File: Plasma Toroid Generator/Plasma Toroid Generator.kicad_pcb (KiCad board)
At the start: 2 copper layers, 66 x 41 mm, 15 parts, among them J1 Conn_01x02, J2 Conn_01x01, J3 Conn_01x01, J4 Conn_01x01, J5 Conn_01x01, Q1 IRFP260

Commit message: Updated PCB layout to fix errors in cap placement
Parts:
- moved C1 4.19 mm to (170.0, 105.4), turned to 180 degrees
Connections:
- C1 pad 1: Net-(C1-Pad1) -> +15V
- J1 pad 1: Net-(C1-Pad1) -> GND
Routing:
- net +15V: track 31.4 -> 45.8 mm
- net Net-(C1-Pad1): track 11.6 -> 0.00 mm
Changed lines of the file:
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@@
   )
   (net 0 "")
-  (net 1 "Net-(C1-Pad1)")
+  (net 1 "Net-(J3-Pad1)")
   (net 2 "GND")
   (net 3 "Net-(C2-Pad1)")
@@
   (net 5 "Net-(D1-Pad1)")
   (net 6 "+15V")
-  (net 7 "Net-(Q1-Pad2)")
-  (net 8 "Net-(R2-Pad2)")
+  (net 7 "Net-(R2-Pad2)")
   (footprint "Capacitor_THT:C_Rect_L7.2mm_W2.5mm_P5.00mm_FKS2_FKP2_MKS2_MKP2" (layer "F.Cu")
     (at 216 111.5 90)
@@
   )
   (footprint "Capacitor_THT:CP_Radial_D10.0mm_P5.00mm" (layer "F.Cu")
-    (at 166 106.632323 -90)
+    (at 170.007677 105.41 180)
     (descr "CP, Radial series, Radial, pin pitch=5.00mm, , diameter=10mm, Electrolytic Capacitor")
     (tags "CP Radial series Radial pin pitch 5.00mm  diameter 10mm Electrolytic Capacitor")
@@
     (property "Sheetname" "")
     (attr through_hole)
-    (fp_text reference "C1" (at 1 -6.25 180) (layer "F.SilkS")
-      (effects (font (size 1 1) (thickness 0.15)))
-    )
-    (fp_text value "10u" (at 2.5 6.25 90) (layer "F.Fab") hide
-      (effects (font (size 1 1) (thickness 0.15)))
-    )
-    (fp_text user "${REFERENCE}" (at 2.5 0 90) (layer "F.Fab")
+    (fp_text reference "C1" (at 1 -6.25 90) (layer "F.SilkS")
+      (effects (font (size 1 1) (thickness 0.15)))
+    )
+    (fp_text value "10u" (at 2.5 6.25) (layer "F.Fab") hide
+      (effects (font (size 1 1) (thickness 0.15)))
+    )
+    (fp_text user "${REFERENCE}" (at 2.5 0) (layer "F.Fab")
       (effects (font (size 1 1) (thickness 0.15)))
     )
@@
     (fp_line (start -1.788861 -2.1875) (end -0.788861 -2.1875) (layer "F.Fab") (width 0.1))
     (fp_circle (center 2.5 0) (end 7.5 0) (layer "F.Fab") (width 0.1) (fill none))
-    (pad "1" thru_hole rect (at 0 0 270) (size 2 2) (drill 1) (layers *.Cu *.Mask)
-      (net 1 "Net-(C1-Pad1)") (pintype "passive"))
-    (pad "2" thru_hole circle (at 5 0 270) (size 2 2) (drill 1) (layers *.Cu *.Mask)
+    (pad "1" thru_hole rect (at 0 0 180) (size 2 2) (drill 1) (layers *.Cu *.Mask)
+      (net 6 "+15V") (pintype "passive"))
+    (pad "2" thru_hole circle (at 5 0 180) (size 2 2) (drill 1) (layers *.Cu *.Mask)
       (net 2 "GND") (pintype "passive"))
     (model "${KICAD6_3DMODEL_DIR}/Capacitor_THT.3dshapes/CP_Radial_D10.0mm_P5.00mm.wrl"
@@
       (net 2 "GND") (pinfunction "1") (pintype "passive"))
     (pad "2" thru_hole circle (at 0 7 270) (size 1.524 1.524) (drill 1) (layers *.Cu *.Mask)
-      (net 8 "Net-(R2-Pad2)") (pinfunction "2") (pintype "passive"))
+      (net 7 "Net-(R2-Pad2)") (pinfunction "2") (pintype "passive"))
     (pad "3" thru_hole circle (at 3.75 7 270) (size 1.524 1.524) (drill 1) (layers *.Cu *.Mask)
       (net 5 "Net-(D1-Pad1)") (pinfunction "3") (pintype "passive"))
@@
     (fp_line (start 0.635 -1.27) (end 1.27 -0.635) (layer "F.Fab") (width 0.1))
     (pad "1" thru_hole rect (at 0 0 180) (size 1.7 1.7) (drill 1) (layers *.Cu *.Mask)
-      (net 7 "Net-(Q1-Pad2)") (pinfunction "Pin_1") (pintype "passive"))
+      (net 1 "Net-(J3-Pad1)") (pinfunction "Pin_1") (pintype "passive"))
     (model "${KICAD6_3DMODEL_DIR}/Connector_PinSocket_2.54mm.3dshapes/PinSocket_1x01_P2.54mm_Vertical.wrl"
       (offset (xyz 0 0 0))
@@
     (fp_line (start 1.27 -0.635) (end 1.27 1.27) (layer "F.Fab") (width 0.1))
     (pad "1" thru_hole rect (at 0 0 180) (size 1.7 1.7) (drill 1) (layers *.Cu *.Mask)
-      (net 7 "Net-(Q1-Pad2)") (pinfunction "Pin_1") (pintype "passive"))
+      (net 1 "Net-(J3-Pad1)") (pinfunction "Pin_1") (pintype "passive"))
     (model "${KICAD6_3DMODEL_DIR}/Connector_PinSocket_2.54mm.3dshapes/PinSocket_1x01_P2.54mm_Vertical.wrl"
       (offset (xyz 0 0 0))
@@
       (net 4 "Net-(C2-Pad2)") (pinfunction "G") (pintype "input"))
     (pad "2" thru_hole oval (at 5.45 0 180) (size 2.5 4.5) (drill 1.5) (layers *.Cu *.Mask)
-      (net 7 "Net-(Q1-Pad2)") (pinfunction "D") (pintype "passive"))
+      (net 1 "Net-(J3-Pad1)") (pinfunction "D") (pintype "passive"))
     (pad "3" thru_hole oval (at 10.9 0 180) (size 2.5 4.5) (drill 1.5) (layers *.Cu *.Mask)
       (net 2 "GND") (pinfunction "S") (pintype "passive"))
@@
     (fp_circle (center 3.5 0) (end 5 0) (layer "F.Fab") (width 0.1) (fill none))
     (pad "1" thru_hole rect (at 0 0 90) (size 2.4 2.4) (drill 1.2) (layers *.Cu *.Mask)
-      (net 1 "Net-(C1-Pad1)") (pinfunction "Pin_1") (pintype "passive"))
+      (net 2 "GND") (pinfunction "Pin_1") (pintype "passive"))
     (pad "2" thru_hole circle (at 3.5 0 90) (size 2.4 2.4) (drill 1.2) (layers *.Cu *.Mask)
       (net 6 "+15V") (pinfunction "Pin_2") (pintype "passive"))
@@
       (net 4 "Net-(C2-Pad2)") (pintype "passive"))
     (pad "2" thru_hole oval (at 15.24 0 180) (size 2.4 2.4) (drill 1.2) (layers *.Cu *.Mask)
-      (net 8 "Net-(R2-Pad2)") (pintype "passive"))
+      (net 7 "Net-(R2-Pad2)") (pintype "passive"))
     (model "${KICAD6_3DMODEL_DIR}/Resistor_THT.3dshapes/R_Axial_DIN0414_L11.9mm_D4.5mm_P15.24mm_Horizontal.wrl"
       (offset (xyz 0 0 0))
@@
     (effects (font (size 1 1) (thickness 0.15)))
   )
-  (segment (start 166.014488 95.000006) (end 166.014488 106.617835) (width 3) (layer "F.Cu") (net 1))
-  (segment (start 166.014488 106.617835) (end 166 106.632323) (width 3) (layer "F.Cu") (net 1))
+  (segment (start 204 92) (end 209 92) (width 3) (layer "F.Cu") (net 1))
+  (segment (start 206 109) (end 206 95) (width 3) (layer "B.Cu") (net 1))
+  (segment (start 213.55 116.55) (end 206 109) (width 3) (layer "B.Cu") (net 1))
+  (segment (start 213.55 124) (end 213.55 116.55) (width 3) (layer "B.Cu") (net 1))
+  (segment (start 206 95) (end 209 92) (width 3) (layer "B.Cu") (net 1))
   (segment (start 205.38 117) (end 205.38 111.62) (width 2.5) (layer "F.Cu") (net 2))
   (segment (start 210.5 106.5) (end 216 106.5) (width 2.5) (layer "F.Cu") (net 2))
@@
   (segment (start 184 106.08) (end 184 111.75) (width 2) (layer "F.Cu") (net 5))
   (segment (start 192 96.62) (end 191.62 97) (width 3) (layer "F.Cu") (net 6))
+  (segment (start 170.007677 92.882323) (end 170.007677 105.41) (width 3) (layer "F.Cu") (net 6))
   (segment (start 191.500006 91.500006) (end 192 92) (width 3) (layer "F.Cu") (net 6))
-  (segment (start 166.014488 91.500006) (end 191.500006 91.500006) (width 3) (layer "F.Cu") (net 6))
+  (segment (start 171.389994 91.500006) (end 170.007677 92.882323) (width 3) (layer "F.Cu") (net 6))
+  (segment (start 166.014488 91.500006) (end 171.389994 91.500006) (width 3) (layer "F.Cu") (net 6))
   (segment (start 192 92) (end 192 96.62) (width 3) (layer "F.Cu") (net 6))
-  (segment (start 204 92) (end 209 92) (width 3) (layer "F.Cu") (net 7))
-  (segment (start 206 109) (end 206 95) (width 3) (layer "B.Cu") (net 7))
-  (segment (start 213.55 116.55) (end 206 109) (width 3) (layer "B.Cu") (net 7))
-  (segment (start 213.55 124) (end 213.55 116.55) (width 3) (layer "B.Cu") (net 7))
-  (segment (start 206 95) (end 209 92) (width 3) (layer "B.Cu") (net 7))
-  (segment (start 180 124) (end 177 121) (width 2) (layer "F.Cu") (net 8))
-  (segment (start 177 121) (end 177 115) (width 2) (layer "F.Cu") (net 8))
-  (segment (start 180.38 124) (end 180 124) (width 2) (layer "F.Cu") (net 8))
-  (segment (start 177 115) (end 180 112) (width 2) (layer "F.Cu") (net 8))
+  (segment (start 171.389994 91.500006) (end 191.500006 91.500006) (width 3) (layer "F.Cu") (net 6))
+  (segment (start 180 124) (end 177 121) (width 2) (layer "F.Cu") (net 7))
+  (segment (start 177 121) (end 177 115) (width 2) (layer "F.Cu") (net 7))
+  (segment (start 180.38 124) (end 180 124) (width 2) (layer "F.Cu") (net 7))
+  (segment (start 177 115) (end 180 112) (width 2) (layer "F.Cu") (net 7))
   (zone (net 2) (net_name "GND") (layer "B.Cu") (hatch edge 0.508)
     (connect_pads yes (clearance 0.508))
@@
         (xy 165 126)
         (xy 161 122)
-        (xy 161 109)
-        (xy 173 109)
+        (xy 161 101.38)
+        (xy 173 101.38)
         (xy 177 105)
         (xy 183 105)

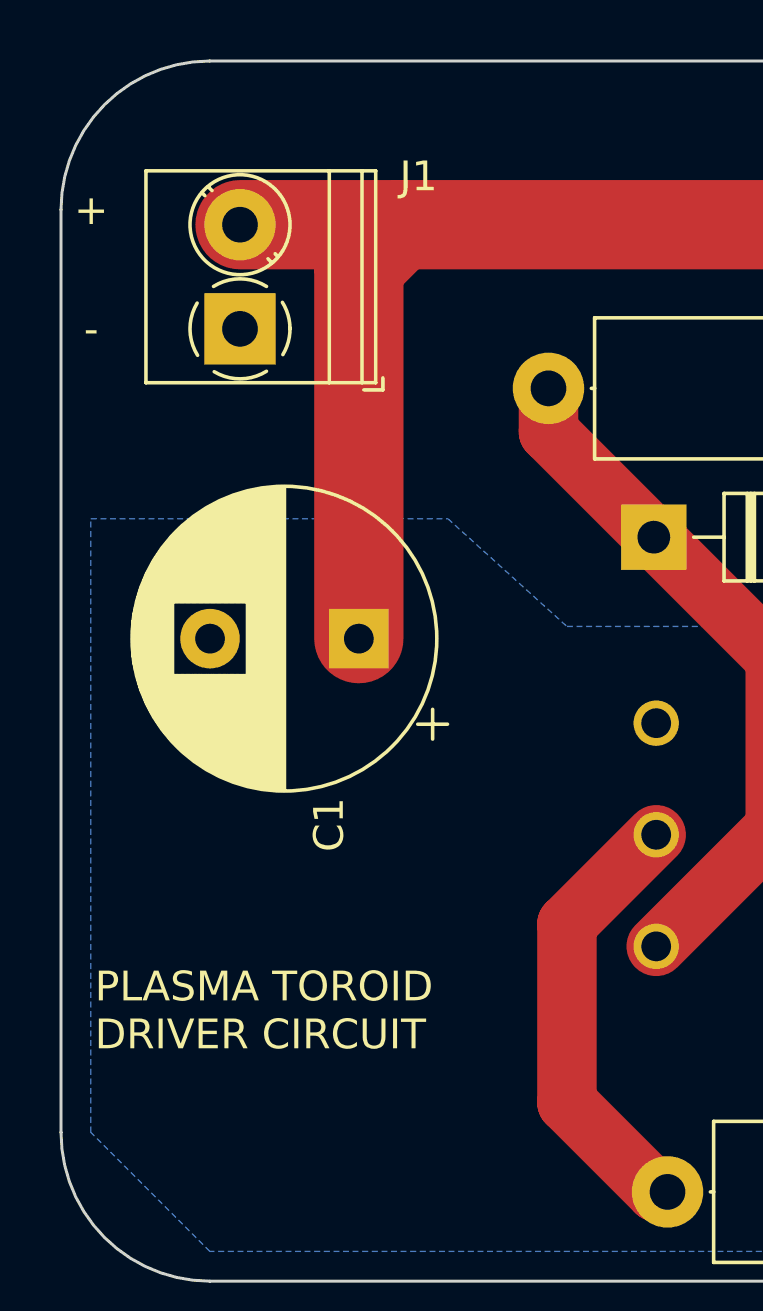
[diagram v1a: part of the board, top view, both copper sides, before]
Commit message: Updates to model to accurately reflect the physical circuit
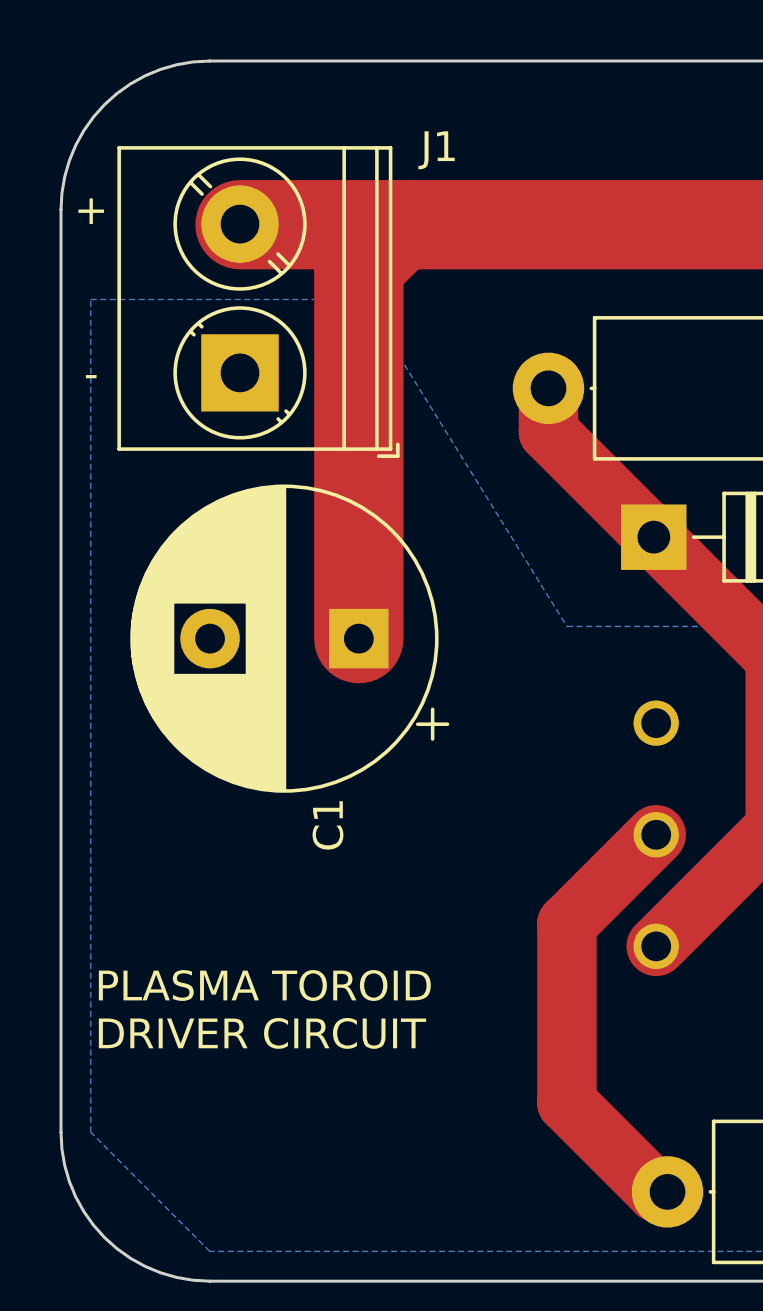
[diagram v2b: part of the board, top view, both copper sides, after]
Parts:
- J1: footprint TerminalBlock_Phoenix:TerminalBlock_Phoenix_PT-1,5-2-3.5-H_1x02_P3.50mm_Horizontal -> TerminalBlock_Phoenix:TerminalBlock_Phoenix_PT-1,5-2-5.0-H_1x02_P5.00mm_Horizontal
- moved J1 1.48 mm to (166.0, 96.5)
